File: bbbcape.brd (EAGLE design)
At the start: 54.6 x 71.8 mm, 28 parts, among them U5V SEEED-MP1584, U6V5 SEEED-MP1584

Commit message: Switched a few pins to confirmed useable pins.
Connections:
- new net AUX_BTN: BBB.75, S1.P$2
- net BAR_GA: no longer S1.P$2
- net FREE: now also BBB.74; no longer BBB.29
- net RESET: now also BBB.68; no longer BBB.27
- net SHLD1: now also BBB.57; no longer BBB.21
- net SHLD2: now also BBB.71; no longer BBB.23
- net SHLD3: now also BBB.73; no longer BBB.25
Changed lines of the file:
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@@
 <signal name="SHLD1">
 <contactref element="SHLD1" pad="3"/>
-<contactref element="BBB" pad="21"/>
-<wire x1="3.81" y1="26.67" x2="-27.94" y2="90.17" width="0" layer="19" extent="1-1"/>
+<contactref element="BBB" pad="57"/>
+<wire x1="-27.94" y1="90.17" x2="52.07" y2="13.97" width="0" layer="19" extent="1-1"/>
 </signal>
 <signal name="SHLD2">
 <contactref element="SHLD1" pad="4"/>
-<contactref element="BBB" pad="23"/>
-<wire x1="3.81" y1="29.21" x2="-25.4" y2="90.17" width="0" layer="19" extent="1-1"/>
+<contactref element="BBB" pad="71"/>
+<wire x1="-25.4" y1="90.17" x2="52.07" y2="31.75" width="0" layer="19" extent="1-1"/>
 </signal>
 <signal name="SHLD3">
 <contactref element="SHLD1" pad="5"/>
-<contactref element="BBB" pad="25"/>
-<wire x1="3.81" y1="31.75" x2="-22.86" y2="90.17" width="0" layer="19" extent="1-1"/>
+<contactref element="BBB" pad="73"/>
+<wire x1="-22.86" y1="90.17" x2="52.07" y2="34.29" width="0" layer="19" extent="1-1"/>
 </signal>
 <signal name="RESET">
 <contactref element="SHLD1" pad="6"/>
-<contactref element="BBB" pad="27"/>
-<wire x1="3.81" y1="34.29" x2="-20.32" y2="90.17" width="0" layer="19" extent="1-1"/>
+<contactref element="BBB" pad="68"/>
+<wire x1="-20.32" y1="90.17" x2="49.53" y2="26.67" width="0" layer="19" extent="1-1"/>
 </signal>
 <signal name="FREE">
 <contactref element="SHLD1" pad="7"/>
-<contactref element="BBB" pad="29"/>
-<wire x1="3.81" y1="36.83" x2="-17.78" y2="90.17" width="0" layer="19" extent="1-1"/>
+<contactref element="BBB" pad="74"/>
+<wire x1="-17.78" y1="90.17" x2="49.53" y2="34.29" width="0" layer="19" extent="1-1"/>
 </signal>
 <signal name="BCOM">
@@
 <contactref element="BPR" pad="5"/>
 <contactref element="BBB" pad="10"/>
-<contactref element="S1" pad="P$2"/>
-<wire x1="1.27" y1="11.43" x2="-77.47" y2="-370.84" width="0" layer="19" extent="1-1"/>
-<wire x1="-31.75" y1="95.25" x2="1.27" y2="11.43" width="0" layer="19" extent="1-1"/>
+<wire x1="1.27" y1="11.43" x2="-31.75" y2="95.25" width="0" layer="19" extent="1-1"/>
 </signal>
 <signal name="3.3V">
@@
 <wire x1="52.07" y1="29.21" x2="-83.82" y2="-294.64" width="0" layer="19" extent="1-1"/>
 </signal>
+<signal name="AUX_BTN">
+<contactref element="BBB" pad="75"/>
+<contactref element="S1" pad="P$2"/>
+<wire x1="52.07" y1="36.83" x2="-77.47" y2="-370.84" width="0" layer="19" extent="1-1"/>
+</signal>
 </signals>

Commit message: PCB done.
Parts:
- moved U5V 457.8 mm to (17.8, 30.5)
- moved U6V5 413.1 mm to (17.8, 11.4)
- moved C3 412.7 mm to (21.6, 47.0)
- moved S1 393.7 mm to (35.6, 5.08)
- moved C2 385.3 mm to (10.2, 41.9), turned to 180 degrees
- moved J1 378.2 mm to (22.9, 50.8), turned to 180 degrees
- moved IRFIZ34E 351.9 mm to (21.6, 44.5)
- moved R9 311.3 mm to (35.6, 12.7), turned to 180 degrees
- moved R8 296.0 mm to (35.6, 15.2)
- moved R7 285.5 mm to (35.6, 22.9), turned to 180 degrees
- moved R6 270.5 mm to (35.6, 25.4)
- moved R5 260.1 mm to (35.6, 33.0)
- moved R4 245.4 mm to (35.6, 35.6), turned to 180 degrees
- moved R3 235.4 mm to (35.6, 43.2)
- moved R2 221.1 mm to (35.6, 45.7), turned to 180 degrees
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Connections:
- removed net N$6: R8.P$2
- new net N$2: R4.P$2, RF_AV_GA.3
- net 5V: now also RF_AR_MI.2, RF_AV_GA.2, RF_AV_MI.2
- net GND: now also RF_AR_MI.1, RF_AV_GA.1, RF_AV_MI.1
- net N$4: now also R6.P$2, RF_AV_MI.3; no longer R4.P$2
- net N$5: now also R8.P$2, RF_AR_MI.3; no longer R6.P$2
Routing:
- net DIR_MOT_DR1: track 0.00 -> 80.9 mm, vias 0 -> 2
- net BCOM: track 0.00 -> 79.2 mm, vias 0 -> 1
- net DIR_MOT_DR0: track 0.00 -> 70.4 mm, vias 0 -> 1
- net VCC: track 0.00 -> 69.8 mm
- net 5V: track 0.00 -> 69.3 mm
- net BAR_DR: track 0.00 -> 66.2 mm
- net BAV_GA: track 0.00 -> 61.6 mm, vias 0 -> 1
- net BAV_DR: track 0.00 -> 60.8 mm, vias 0 -> 1
- net BAR_GA: track 0.00 -> 60.7 mm, vias 0 -> 1
- net VDD: track 0.00 -> 59.1 mm, vias 0 -> 2
- net VBAT: track 0.00 -> 52.6 mm
- net DIR_MOT_GA0: track 0.00 -> 52.3 mm, vias 0 -> 1
- net PWM_MOT_DR: track 0.00 -> 51.4 mm, vias 0 -> 1
- net AIN3: track 0.00 -> 49.0 mm, vias 0 -> 1
- net FEU: track 0.00 -> 48.9 mm, vias 0 -> 1
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- added copper zone on layer 1, net GND
- added copper zone on layer 16, net GND
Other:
- board text added: "+"
- board text added: "-"
- board text added: "1"
- board text added: "2016-12-15"
- board text added: "BBBCape 0.1.1"
- board text added: "Michel Lavoie"
- board text added: "s"

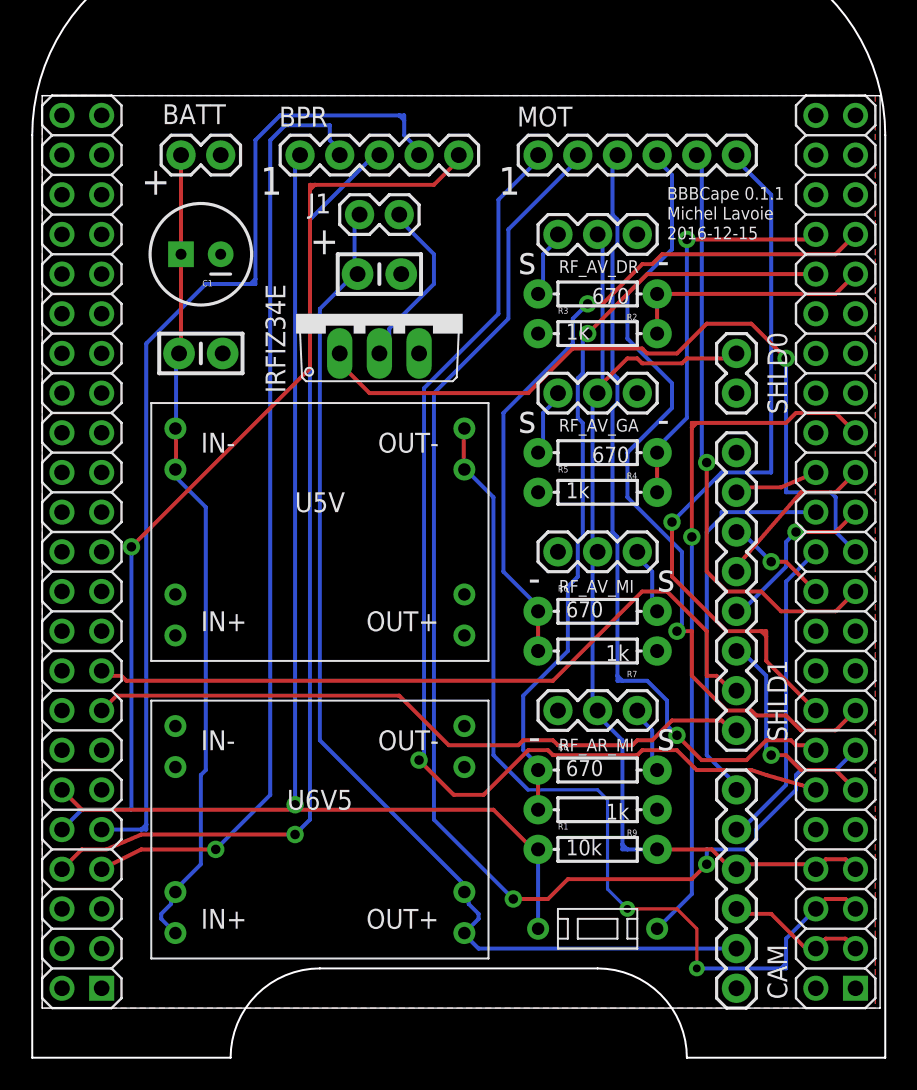
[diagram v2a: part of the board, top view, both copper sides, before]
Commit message: Trying to reduce the board overall dimensions, no success...
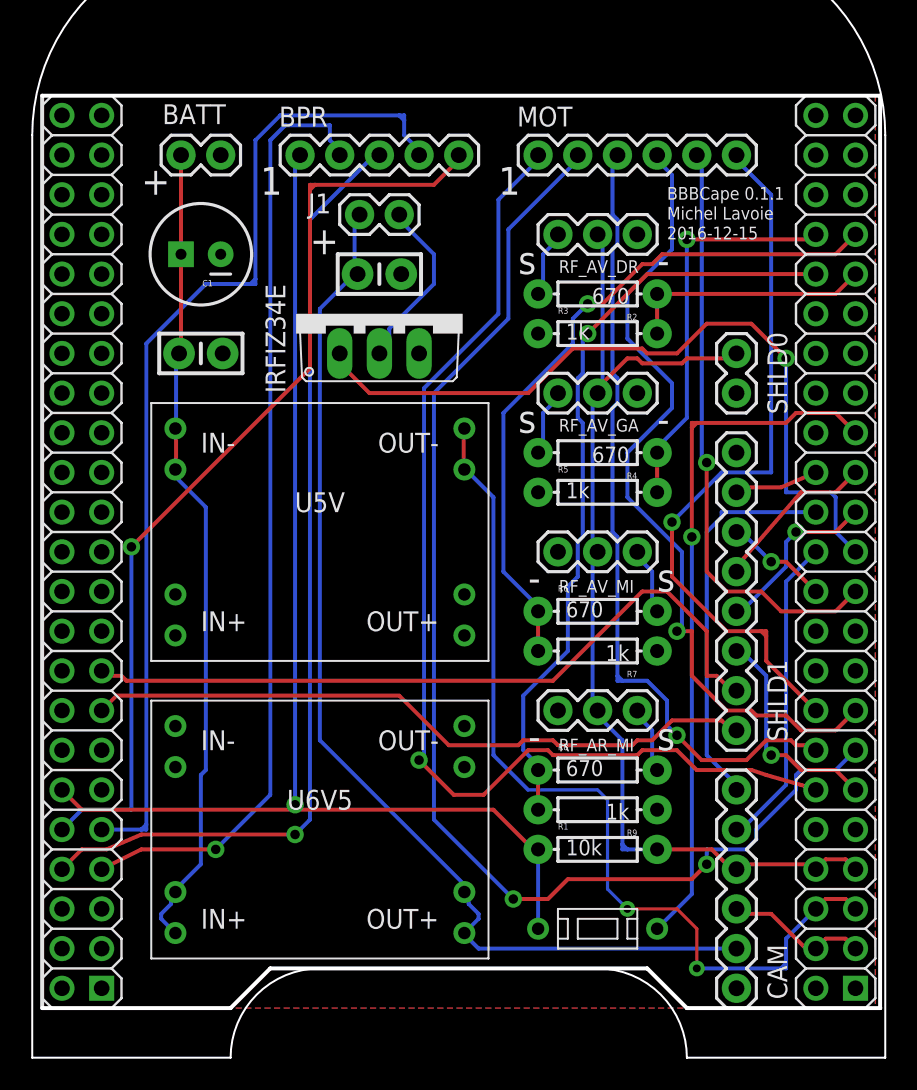
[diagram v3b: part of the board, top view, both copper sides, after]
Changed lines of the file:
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@@
 <board>
 <plain>
-<wire x1="0" y1="0" x2="53.645" y2="0" width="0" layer="20"/>
-<wire x1="53.645" y1="0" x2="53.645" y2="58.41" width="0" layer="20"/>
-<wire x1="53.645" y1="58.41" x2="0" y2="58.41" width="0" layer="20"/>
-<wire x1="0" y1="58.41" x2="0" y2="0" width="0" layer="20"/>
+<wire x1="53.645" y1="0" x2="53.645" y2="58.41" width="0.254" layer="20"/>
+<wire x1="53.645" y1="58.41" x2="0" y2="58.41" width="0.254" layer="20"/>
+<wire x1="0" y1="58.41" x2="0" y2="0" width="0.254" layer="21"/>
 <text x="6.35" y="52.07" size="1.778" layer="21">+</text>
 <text x="13.97" y="52.07" size="1.778" layer="21">1</text>
@@
 <text x="40.005" y="50.4825" size="0.8128" layer="21">Michel Lavoie</text>
 <text x="40.005" y="49.2125" size="0.8128" layer="21">2016-12-15</text>
+<wire x1="0" y1="0" x2="12.065" y2="0" width="0.254" layer="20"/>
+<wire x1="12.065" y1="0" x2="14.605" y2="2.54" width="0.254" layer="20"/>
+<wire x1="14.605" y1="2.54" x2="38.735" y2="2.54" width="0.254" layer="20"/>
+<wire x1="38.735" y1="2.54" x2="41.275" y2="0" width="0.254" layer="20"/>
+<wire x1="41.275" y1="0" x2="53.6575" y2="0" width="0.254" layer="20"/>
 </plain>
 <attributes>
